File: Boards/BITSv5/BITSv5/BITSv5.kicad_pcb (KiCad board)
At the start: 4 copper layers, 54 x 59.5 mm, 80 parts, among them J1 Conn_01x10_Pin, J2 USB_C_Receptacle_USB2.0, J3 Conn_01x07, Q1 Q_NMOS_GSD, Q2 Q_PMOS_GSD, SW3 SLIDE, U1 MCU_RaspberryPi_RP2040_RP2040, U10 USBLC6-2SC6, U2 W25Q128JVS, U3 MAX-M10S, U4 MAX25255AFDA/VY+, U6 XBee_SMT, U7 TPS2121RUXR, U8 LT6703CDC-3, U9 TVS1800DRVR, Y1 12MHz

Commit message: BITSv5 board done
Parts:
- moved AE1 0.46 mm to (190.1, 103.1)
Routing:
- net GND: track 149.7 -> 119.7 mm, vias 62 -> 82
- net VCC: track 38.9 -> 13.7 mm, vias 7 -> 9
- net /IRIDIUM_TXD: track 13.9 -> 27.1 mm, vias 1 -> 0
- net +3V3: track 83.1 -> 76.0 mm, vias 22 -> 21
- net Net-(AE1-A): track 5.45 -> 11.8 mm
- net Net-(SW3-C): track 62.6 -> 59.5 mm, vias 2 -> 3
- net +5V: track 41.2 -> 42.7 mm, vias 6 -> 7
- net /XBEE_RTS: track 47.8 -> 49.1 mm
- net /GPS_SDA: track 25.0 -> 23.9 mm
- net /GPS_SCL: track 22.6 -> 21.5 mm
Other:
- board size 54 x 59.5 mm -> 63.7 x 59.5 mm

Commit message: xbee joint and bits updates
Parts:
- R17: value 51.1K -> 46.4K
- R18: value 1.05M -> 1.5M
- R19: value 154K -> 100K
- moved AE1 1.58 mm to (188.5, 103.1)
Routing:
- net +1V1: track 10.2 -> 32.2 mm, vias 1 -> 3
- net Net-(AE1-A): track 11.8 -> 10.2 mm
- net GND: track 119.7 -> 119.6 mm, vias 82 -> 109
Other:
- board size 63.7 x 59.5 mm -> 61.7 x 59.5 mm
- board text added: "A. Takeuchi J. Molter"
- board text added: "BITSv5.0 09/23"
- board text added: "J. Bishop M. Shipman"

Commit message: added button to BITS5
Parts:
- added SW1: SW_Push, Button_Switch_SMD:SW_Push_1P1T-SH_NO_CK_KMR2xxG, F.Cu at (167.6, 113.5)
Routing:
- net GND: track 119.6 -> 125.3 mm, vias 109 -> 110
- net Net-(Q2-D): track 15.5 -> 21.1 mm
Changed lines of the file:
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@@
       (net 4 "GND") (pinfunction "PAD") (pintype "unspecified"))
   )
+  (footprint "Button_Switch_SMD:SW_Push_1P1T-SH_NO_CK_KMR2xxG" (layer "F.Cu")
+    (at 167.6 113.5)
+    (descr "CK components KMR2 tactile switch with ground pin http://www.ckswitches.com/media/1479/kmr2.pdf")
+    (tags "tactile switch kmr2")
+    (property "Sheetfile" "BITSv5.kicad_sch")
+    (property "Sheetname" "")
+    (property "ki_description" "Push button switch, generic, two pins")
+    (property "ki_keywords" "switch normally-open pushbutton push-button")
+    (attr smd)
+    (fp_text reference "SW1" (at 0 -2.45) (layer "F.SilkS")
+        (effects (font (size 0.8 0.8) (thickness 0.15)))
+    )
+    (fp_text value "SW_Push" (at 0 2.55) (layer "F.Fab")
+        (effects (font (size 1 1) (thickness 0.15)))
+    )
+    (fp_text user "${REFERENCE}" (at 0 -2.45) (layer "F.Fab")
+        (effects (font (size 1 1) (thickness 0.15)))
+    )
+    (fp_line (start -2.2 0.05) (end -2.2 -0.05)
+      (stroke (width 0.12) (type solid)) (layer "F.SilkS"))
+    (fp_line (start -2.2 1.55) (end 2.2 1.55)
+      (stroke (width 0.12) (type solid)) (layer "F.SilkS"))
+    (fp_line (start -1.15 -1.55) (end -2.2 -1.55)
+      (stroke (width 0.12) (type solid)) (layer "F.SilkS"))
+    (fp_line (start 2.2 -1.55) (end 1.15 -1.55)
+      (stroke (width 0.12) (type solid)) (layer "F.SilkS"))
+    (fp_line (start 2.2 0.05) (end 2.2 -0.05)
+      (stroke (width 0.12) (type solid)) (layer "F.SilkS"))
+    (fp_line (start -2.8 -1.8) (end 2.8 -1.8)
+      (stroke (width 0.05) (type solid)) (layer "F.CrtYd"))
+    (fp_line (start -2.8 1.8) (end -2.8 -1.8)
+      (stroke (width 0.05) (type solid)) (layer "F.CrtYd"))
+    (fp_line (start 2.8 -1.8) (end 2.8 1.8)
+      (stroke (width 0.05) (type solid)) (layer "F.CrtYd"))
+    (fp_line (start 2.8 1.8) (end -2.8 1.8)
+      (stroke (width 0.05) (type solid)) (layer "F.CrtYd"))
+    (fp_line (start -2.1 -1.4) (end 2.1 -1.4)
+      (stroke (width 0.1) (type solid)) (layer "F.Fab"))
+    (fp_line (start -2.1 1.4) (end -2.1 -1.4)
+      (stroke (width 0.1) (type solid)) (layer "F.Fab"))
+    (fp_line (start 2.1 -1.4) (end 2.1 1.4)
+      (stroke (width 0.1) (type solid)) (layer "F.Fab"))
+    (fp_line (start 2.1 1.4) (end -2.1 1.4)
+      (stroke (width 0.1) (type solid)) (layer "F.Fab"))
+    (fp_circle (center 0 0) (end 0 0.8)
+      (stroke (width 0.1) (type solid)) (fill none) (layer "F.Fab"))
+    (pad "1" smd rect (at -2.05 -0.8) (size 0.9 1) (layers "F.Cu" "F.Paste" "F.Mask")
+      (net 4 "GND") (pinfunction "1") (pintype "passive"))
+    (pad "1" smd rect (at 2.05 -0.8) (size 0.9 1) (layers "F.Cu" "F.Paste" "F.Mask")
+      (net 4 "GND") (pinfunction "1") (pintype "passive"))
+    (pad "2" smd rect (at -2.05 0.8) (size 0.9 1) (layers "F.Cu" "F.Paste" "F.Mask")
+      (net 100 "Net-(Q2-D)") (pinfunction "2") (pintype "passive"))
+    (pad "2" smd rect (at 2.05 0.8) (size 0.9 1) (layers "F.Cu" "F.Paste" "F.Mask")
+      (net 100 "Net-(Q2-D)") (pinfunction "2") (pintype "passive"))
+    (pad "SH" smd rect (at 0 -1.425) (size 1.7 0.55) (layers "F.Cu" "F.Paste" "F.Mask"))
+    (model "${KICAD6_3DMODEL_DIR}/Button_Switch_SMD.3dshapes/SW_Push_1P1T-SH_NO_CK_KMR2xxG.wrl"
+      (offset (xyz 0 0 0))
+      (scale (xyz 1 1 1))
+      (rotate (xyz 0 0 0))
+    )
+  )
   (footprint "Resistor_SMD:R_0603_1608Metric_Pad0.98x0.95mm_HandSolder" (layer "F.Cu")
     (at 156.3 84.314999 180)
@@
     (property "ki_keywords" "cap capacitor")
     (attr smd)
-    (fp_text reference "C1" (at 1.12 1.445 180) (layer "F.SilkS")
+    (fp_text reference "C1" (at 1.36 1.5 180) (layer "F.SilkS")
         (effects (font (size 0.75 0.75) (thickness 0.125)))
     )
@@
   (segment (start 156.055 111.65) (end 157.055 110.65) (width 0.2) (layer "F.Cu") (net 4))
   (segment (start 178.57675 72.49075) (end 179.94 73.854) (width 0.5) (layer "F.Cu") (net 4))
+  (segment (start 169.65 112.7) (end 165.55 112.7) (width 0.25) (layer "F.Cu") (net 4))
   (segment (start 134.991899 103.068101) (end 134.991899 104.71) (width 0.5) (layer "F.Cu") (net 4))
   (segment (start 160.8 77.227499) (end 159.6625 77.227499) (width 0.5) (layer "F.Cu") (net 4))
@@
   (segment (start 159.6625 77.227499) (end 159.425 77.464999) (width 0.5) (layer "F.Cu") (net 4))
   (segment (start 176.34 114) (end 174.009998 116.330002) (width 0.5) (layer "F.Cu") (net 4))
+  (segment (start 170.7 112.7) (end 171.1 113.1) (width 0.25) (layer "F.Cu") (net 4))
   (segment (start 158.655 119.7) (end 157.34 118.385) (width 0.3) (layer "F.Cu") (net 4))
   (segment (start 153.2375 77.789999) (end 153.2625 77.764999) (width 0.5) (layer "F.Cu") (net 4))
@@
   (segment (start 151.185001 66.205001) (end 151.185001 67.242499) (width 0.5) (layer "F.Cu") (net 4))
   (segment (start 149.210001 66.260001) (end 149.210001 67.242499) (width 0.5) (layer "F.Cu") (net 4))
+  (segment (start 169.65 112.7) (end 170.7 112.7) (width 0.25) (layer "F.Cu") (net 4))
   (segment (start 180.31675 66.83825) (end 180.31925 66.84075) (width 0.5) (layer "F.Cu") (net 4))
   (segment (start 151.852501 80.88) (end 146.86 80.88) (width 1) (layer "F.Cu") (net 4))
@@
   (via (at 170.14 74.9) (size 0.5) (drill 0.3) (layers "F.Cu" "B.Cu") (free) (net 4))
   (via (at 175.31 100.94) (size 0.5) (drill 0.3) (layers "F.Cu" "B.Cu") (free) (net 4))
+  (via (at 171.1 113.1) (size 0.8) (drill 0.4) (layers "F.Cu" "B.Cu") (net 4))
   (via (at 182.45 102.09) (size 0.5) (drill 0.3) (layers "F.Cu" "B.Cu") (free) (net 4))
   (via (at 166.06 71.92) (size 0.5) (drill 0.3) (layers "F.Cu" "B.Cu") (free) (net 4))
@@
   (segment (start 151.1925 81.7675) (end 149.93 83.03) (width 0.4) (layer "B.Cu") (net 91))
   (segment (start 159.513263 113.9) (end 161.69 113.9) (width 0.2) (layer "F.Cu") (net 100))
+  (segment (start 165.55 114.3) (end 165.98875 114.3) (width 0.25) (layer "F.Cu") (net 100))
   (segment (start 161.69 113.9) (end 162.21 113.38) (width 0.2) (layer "F.Cu") (net 100))
+  (segment (start 169.65 114.3) (end 169.58875 114.3) (width 0.25) (layer "F.Cu") (net 100))
   (segment (start 167.78875 116.1) (end 167.78875 117.2875) (width 0.5) (layer "F.Cu") (net 100))
+  (segment (start 165.98875 114.3) (end 167.78875 116.1) (width 0.25) (layer "F.Cu") (net 100))
   (segment (start 167.78875 117.2875) (end 164.80125 117.2875) (width 0.5) (layer "F.Cu") (net 100))
   (segment (start 164.80125 117.2875) (end 164.53875 117.55) (width 0.5) (layer "F.Cu") (net 100))
+  (segment (start 169.58875 114.3) (end 167.78875 116.1) (width 0.25) (layer "F.Cu") (net 100))
   (segment (start 158.855 113.241737) (end 159.513263 113.9) (width 0.2) (layer "F.Cu") (net 100))
   (segment (start 158.855 112.8125) (end 158.855 113.241737) (width 0.2) (layer "F.Cu") (net 100))

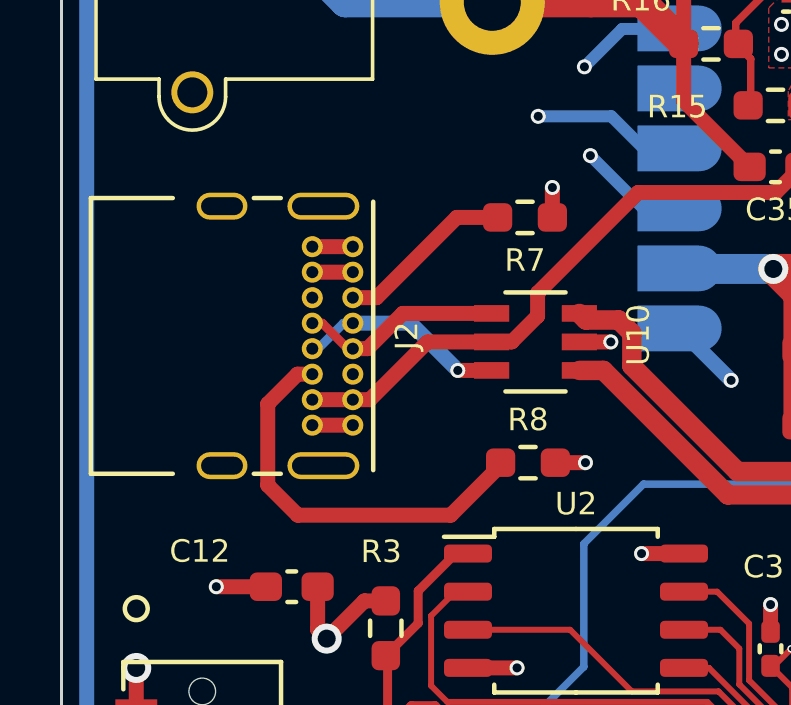
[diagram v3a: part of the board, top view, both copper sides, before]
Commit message: BITSv5 USB change
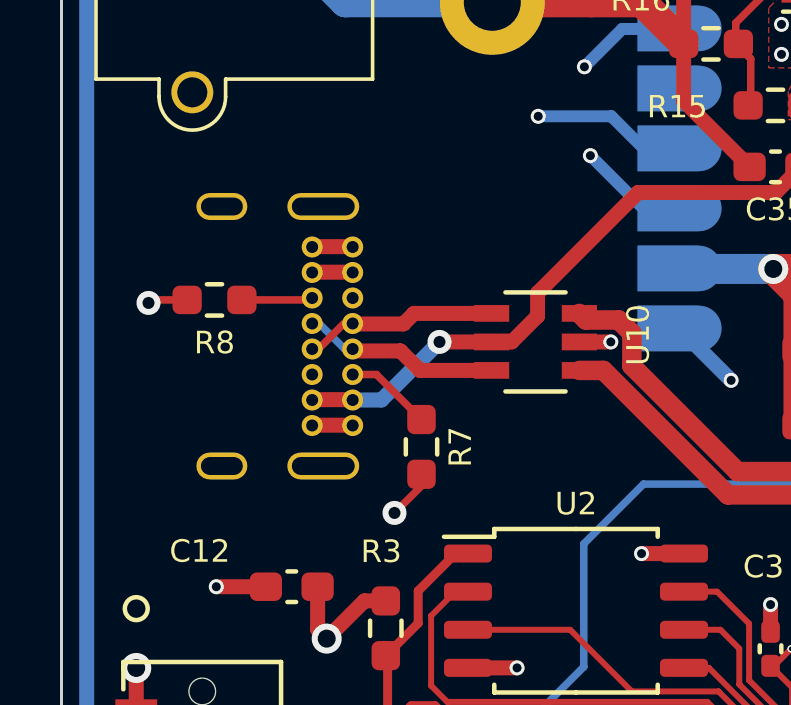
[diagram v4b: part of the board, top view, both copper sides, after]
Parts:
- J2: moved to B.Cu
- moved R8 11.8 mm to (137.6, 90.8), turned to 180 degrees
- moved R7 8.39 mm to (144.5, 95.7), turned to 90 degrees
- moved J2 5.96 mm to (142.2, 95.0), turned to 90 degrees
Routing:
- net Net-(J2-CC2): track 13.6 -> 2.37 mm
- net Net-(J2-CC1): track 6.02 -> 2.92 mm
- net GND: track 125.3 -> 126.3 mm
- net VBUS: track 29.6 -> 29.2 mm, vias 0 -> 1
- net Net-(J2-D+-PadA6): track 6.98 -> 6.63 mm, vias 1 -> 0

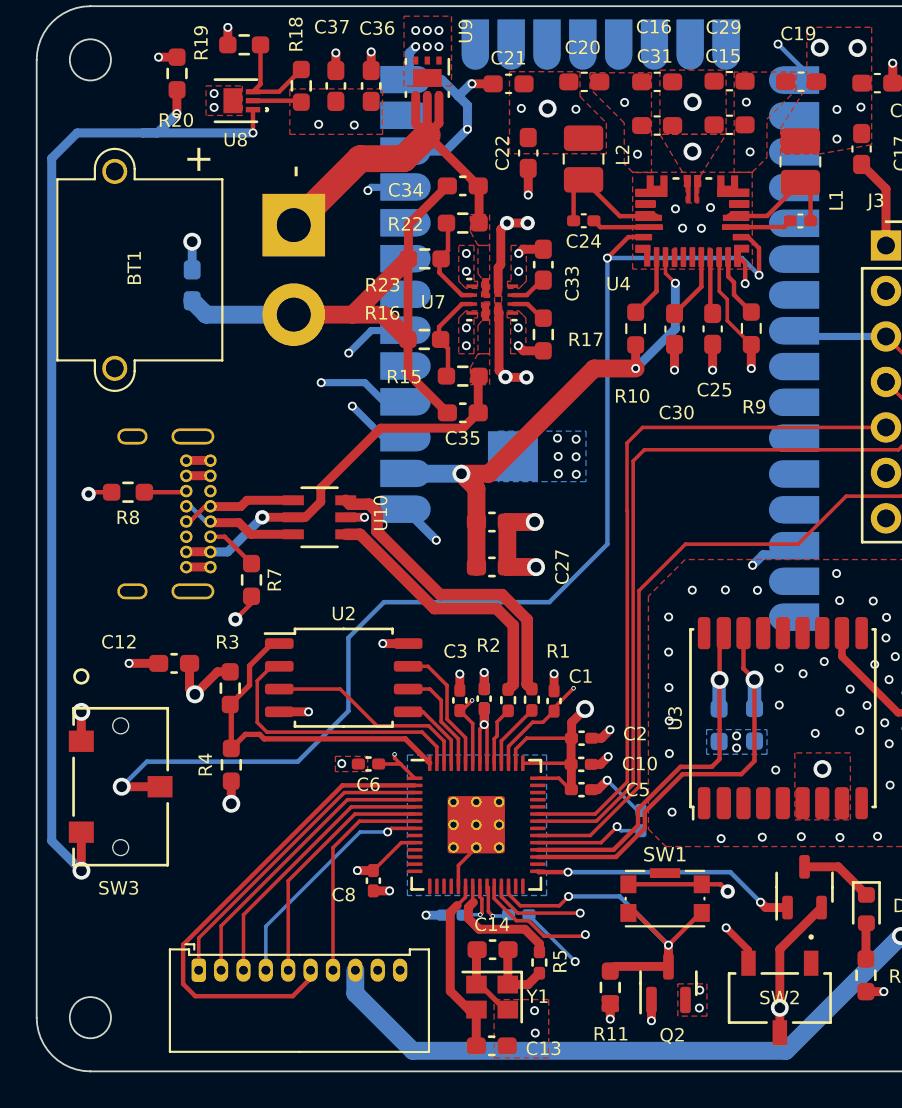
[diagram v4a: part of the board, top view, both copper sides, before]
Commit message: BITSv5 added additional Xbee connector
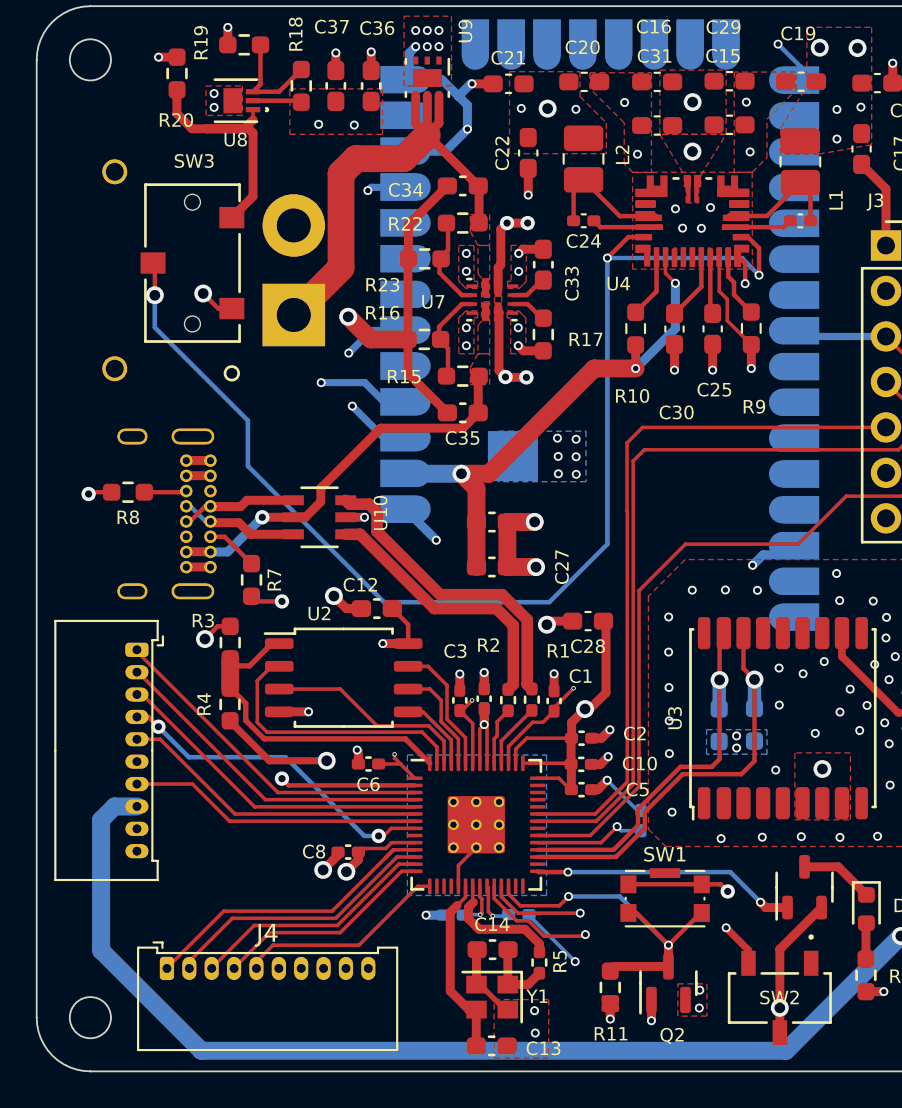
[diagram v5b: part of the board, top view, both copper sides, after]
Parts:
- added J4: Conn_01x10_Pin, Connector_Molex:Molex_PicoBlade_53048-1010_1x10_P1.25mm_Horizontal, F.Cu at (139.8, 117.4)
- BT1: moved to B.Cu
- C28: moved to F.Cu
- moved SW3 29.5 mm to (141.2, 78.0), turned to 90 degrees
- moved C28 29.0 mm to (163.3, 98.0), turned to 180 degrees
- moved J1 18.2 mm to (138.1, 99.6), turned to -90 degrees
- moved C12 11.7 mm to (151.5, 97.3)
- moved BT1 5.02 mm to (146.9, 80.9), turned to -90 degrees
- moved R4 3.37 mm to (143.3, 102.7)
- moved R3 2.55 mm to (143.3, 99.2)
- moved C8 2.13 mm to (149.9, 110.9), turned to 180 degrees
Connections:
- U1 pad 11: unconnected-(U1-GPIO8-Pad11) -> /2.4_MISO
- U1 pad 12: unconnected-(U1-GPIO9-Pad12) -> /2.4_SSEL
- U1 pad 13: unconnected-(U1-GPIO10-Pad13) -> /2.4_SCLK
- U1 pad 14: unconnected-(U1-GPIO11-Pad14) -> /2.4_MOSI
- U1 pad 15: unconnected-(U1-GPIO12-Pad15) -> /2.4_ATTN
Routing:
- net Net-(SW3-C): track 59.5 -> 17.3 mm, vias 3 -> 0
- net +5V: track 42.7 -> 66.2 mm
- net /2.4_MISO: track 0.00 -> 17.2 mm
- net /2.4_SSEL: track 0.00 -> 15.0 mm
- net /2.4_SCLK: track 0.00 -> 13.8 mm
- net GND: track 126.3 -> 112.9 mm, vias 110 -> 112
- net /2.4_MOSI: track 0.00 -> 12.4 mm
- net /2.4_ATTN: track 0.00 -> 11.8 mm
- net /IRIDIUM_TXD: track 27.1 -> 16.1 mm, vias 0 -> 1
- net Net-(SW2-B): track 52.0 -> 61.7 mm
- net /IRIDIUM_NETAV: track 13.0 -> 18.4 mm, vias 1 -> 2
- net +BATT: track 22.8 -> 28.0 mm
- net +3V3: track 76.0 -> 80.6 mm, vias 21 -> 20
- net /IRIDIUM_ON/OFF: track 12.0 -> 16.4 mm
- net /IRIDIUM_RING: track 13.6 -> 17.2 mm
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
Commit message: bits v5 w/ dorji radio
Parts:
- removed C31: 0.1uF, Capacitor_SMD:C_0603_1608Metric_Pad1.08x0.95mm_HandSolder
- removed J4: Conn_01x10_Pin, Connector_Molex:Molex_PicoBlade_53048-1010_1x10_P1.25mm_Horizontal
- removed Q2: Q_PMOS_GSD, Package_TO_SOT_SMD:SOT-23
- added AE2: Antenna, BITSv5:ANT_0915AT43A0026E_JOT, F.Cu at (150.4, 73.0)
- added BT2: 3V, BITSv5:SEIKO_ML414H_IV01E, B.Cu at (148.7, 51.4)
- added C38: 15uF, Capacitor_SMD:C_1206_3216Metric, F.Cu at (149.5, 61.7)
- added C39: 1uF, Capacitor_SMD:C_0603_1608Metric, F.Cu at (140.5, 46.9)
- added C40: 1uF, Capacitor_SMD:C_0603_1608Metric, F.Cu at (138.9, 46.9)
- added C41: 1uF, Capacitor_SMD:C_0603_1608Metric, F.Cu at (134.6, 75.2)
- added C42: 100nF, Capacitor_SMD:C_0603_1608Metric, F.Cu at (141.2, 74.5)
- added C43: 200nF, Capacitor_SMD:C_0603_1608Metric, F.Cu at (141.2, 72.9)
- added D2: 0.5A/40V/240mV, Diode_SMD:D_SOD-123F, F.Cu at (147.4, 52.1)
- added H1: M2, MountingHole:MountingHole_2.2mm_M2_Pad, F.Cu at (108.2, 45.2)
- added H2: M2, MountingHole:MountingHole_2.2mm_M2_Pad, F.Cu at (108.2, 84.2)
- added H3: M2, MountingHole:MountingHole_2.2mm_M2_Pad, F.Cu at (149.2, 84.2)
- added H4: M2, MountingHole:MountingHole_2.2mm_M2_Pad, F.Cu at (149.2, 45.2)
- added L3: 3.3uH, Inductor_SMD:L_1210_3225Metric, F.Cu at (146.0, 56.1)
- added L4: 3.3uH, Inductor_SMD:L_1210_3225Metric, F.Cu at (145.9, 62.4)
- added R13: 100m, Resistor_SMD:R_0603_1608Metric, F.Cu at (145.1, 60.0)
- added R14: 3.3K, Resistor_SMD:R_0603_1608Metric, F.Cu at (149.4, 51.4)
- added R27: 22.1K, Resistor_SMD:R_0603_1608Metric, F.Cu at (139.2, 52.1)
- added R29: 100K, Resistor_SMD:R_0603_1608Metric, F.Cu at (137.3, 61.6)
- added R32: 34.8K, Resistor_SMD:R_0603_1608Metric, F.Cu at (135.2, 52.2)
- added R33: 100K, Resistor_SMD:R_0603_1608Metric, F.Cu at (135.7, 61.6)
- added R34: 15K, Resistor_SMD:R_0603_1608Metric, F.Cu at (133.2, 55.4)
- added R6: 10K, Resistor_SMD:R_0603_1608Metric, B.Cu at (116.1, 81.7)
- added U11: MS5607-02BA, Package_LGA:LGA-8_3x5mm_P1.25mm, B.Cu at (117.7, 79.0)
- added U5: LT8653SIV-PBF, BITSv5:LT8653SIV-PBF, F.Cu at (137.2, 57.8)
- AE1, R7, R8, U3: moved to B.Cu
- BT1: moved to F.Cu
- C1, C10, C2, C3, C5, C6, C7, C8: footprint Capacitor_SMD:C_0402_1005Metric_Pad0.74x0.62mm_HandSolder -> Capacitor_SMD:C_0402_1005Metric
- C11, C32, C4, C9: footprint Capacitor_SMD:C_0402_1005Metric_Pad0.74x0.62mm_HandSolder -> Capacitor_SMD:C_0402_1005Metric; moved to F.Cu
- C12, C13, C14, C37: footprint Capacitor_SMD:C_0603_1608Metric_Pad1.08x0.95mm_HandSolder -> Capacitor_SMD:C_0402_1005Metric
- C15: value 0.1uF -> 4.7uF; footprint Capacitor_SMD:C_0603_1608Metric_Pad1.08x0.95mm_HandSolder -> Capacitor_SMD:C_0603_1608Metric
- C16: value 4.7uF -> 47uF; footprint Capacitor_SMD:C_0603_1608Metric_Pad1.08x0.95mm_HandSolder -> Capacitor_SMD:C_1206_3216Metric
- C17: value 22uF -> 4.7pF; footprint Capacitor_SMD:C_0603_1608Metric_Pad1.08x0.95mm_HandSolder -> Capacitor_SMD:C_0603_1608Metric
- C18, C21: value 22uF -> 470pF; footprint Capacitor_SMD:C_0603_1608Metric_Pad1.08x0.95mm_HandSolder -> Capacitor_SMD:C_0603_1608Metric
- C19: value 22uF -> 10nF; footprint Capacitor_SMD:C_0603_1608Metric_Pad1.08x0.95mm_HandSolder -> Capacitor_SMD:C_0603_1608Metric
- C20: value 22uF -> 100uF; footprint Capacitor_SMD:C_0603_1608Metric_Pad1.08x0.95mm_HandSolder -> Capacitor_SMD:C_1206_3216Metric
- C22: value 22uF -> 100nF; footprint Capacitor_SMD:C_0603_1608Metric_Pad1.08x0.95mm_HandSolder -> Capacitor_SMD:C_0603_1608Metric
- C23: value 0.1uF -> 4.7pF; footprint Capacitor_SMD:C_0402_1005Metric_Pad0.74x0.62mm_HandSolder -> Capacitor_SMD:C_0603_1608Metric
- C24: value 0.1uF -> 10nF; footprint Capacitor_SMD:C_0402_1005Metric_Pad0.74x0.62mm_HandSolder -> Capacitor_SMD:C_0603_1608Metric
- C25: value 2.2uF -> 1uF; footprint Capacitor_SMD:C_0603_1608Metric_Pad1.08x0.95mm_HandSolder -> Capacitor_SMD:C_0603_1608Metric
- C26: value 100pF -> 10uF; footprint Capacitor_SMD:C_0603_1608Metric_Pad1.08x0.95mm_HandSolder -> Capacitor_SMD:C_0603_1608Metric
- C27, C33, C34, C35, C36: footprint Capacitor_SMD:C_0603_1608Metric_Pad1.08x0.95mm_HandSolder -> Capacitor_SMD:C_0603_1608Metric
- C28: value 10uF -> 15uF; footprint Capacitor_SMD:C_0603_1608Metric_Pad1.08x0.95mm_HandSolder -> Capacitor_SMD:C_1206_3216Metric
- C29: value 4.7uF -> 100nF; footprint Capacitor_SMD:C_0603_1608Metric_Pad1.08x0.95mm_HandSolder -> Capacitor_SMD:C_0603_1608Metric; moved to B.Cu
- C30: value 4.7uF -> 100nF; footprint Capacitor_SMD:C_0603_1608Metric_Pad1.08x0.95mm_HandSolder -> Capacitor_SMD:C_0603_1608Metric
- J1: footprint Connector_Molex:Molex_PicoBlade_53048-1010_1x10_P1.25mm_Horizontal -> Connector_Molex:Molex_PicoBlade_53261-1071_1x10-1MP_P1.25mm_Horizontal
- J2: footprint Connector_USB:USB_C_Receptacle_GCT_USB4085 -> Connector_USB:USB_C_Receptacle_GCT_USB4105-xx-A_16P_TopMnt_Horizontal; moved to F.Cu
- J3: value Conn_01x07 -> SOICbite; footprint Connector_PinSocket_2.54mm:PinSocket_1x07_P2.54mm_Vertical -> BITSv5:SOIC_clipProgSmall
- L1, L2: value 0.47uH -> 2.2uH; footprint Inductor_SMD:L_1008_2520Metric_Pad1.43x2.20mm_HandSolder -> Inductor_SMD:L_1210_3225Metric
- R1, R2: value 27Ω -> 27; footprint Resistor_SMD:R_0402_1005Metric_Pad0.72x0.64mm_HandSolder -> Resistor_SMD:R_0402_1005Metric
- R10: value 10K -> 100m; footprint Resistor_SMD:R_0603_1608Metric_Pad0.98x0.95mm_HandSolder -> Resistor_SMD:R_0603_1608Metric
- R11: value 10K -> 100K; footprint Resistor_SMD:R_0603_1608Metric_Pad0.98x0.95mm_HandSolder -> Resistor_SMD:R_0603_1608Metric
- R12, R15, R16, R22, R23, R4: footprint Resistor_SMD:R_0603_1608Metric_Pad0.98x0.95mm_HandSolder -> Resistor_SMD:R_0603_1608Metric
- R17: value 46.4K -> 44.2K; footprint Resistor_SMD:R_0603_1608Metric_Pad0.98x0.95mm_HandSolder -> Resistor_SMD:R_0603_1608Metric
- R18, R19, R20: footprint Resistor_SMD:R_0603_1608Metric_Pad0.98x0.95mm_HandSolder -> Resistor_SMD:R_0402_1005Metric
- R21, R24: footprint Resistor_SMD:R_0603_1608Metric_Pad0.98x0.95mm_HandSolder -> Resistor_SMD:R_0603_1608Metric; moved to F.Cu
- R3: value 10K -> DNF; footprint Resistor_SMD:R_0603_1608Metric_Pad0.98x0.95mm_HandSolder -> Resistor_SMD:R_0603_1608Metric
- R5: footprint Resistor_SMD:R_0402_1005Metric_Pad0.72x0.64mm_HandSolder -> Capacitor_SMD:C_0402_1005Metric
- R9: footprint Resistor_SMD:R_0603_1608Metric_Pad0.98x0.95mm_HandSolder -> Resistor_SMD:R_0603_1608Metric; moved to B.Cu
- U10: footprint BITSv5:SOT23-6L_STM-M -> BITSv5:SOT23-6L_STM
- U2: footprint Package_SO:SOIC-8_5.23x5.23mm_P1.27mm -> BITSv5:WSON_128JVPIQ_WIN
- U4: value MAX25255AFDA/VY+ -> DRF1262TL; footprint BITSv5:21-100477_90-100168_MXM -> BITSv5:DRF1262TL; moved to B.Cu
- U6: value XBee_SMT -> TPS2121RUXR; footprint BITSv5:XCVR_XBP9X-DMUS-001 -> BITSv5:TPS2121; moved to F.Cu
- U7: value TPS2121RUXR -> MAX6747KA29+T; footprint BITSv5:TPS2121 -> BITSv5:21-0078H_MXM
- moved AE1 85.5 mm to (126.6, 44.2), turned to 180 degrees
- moved R12 75.1 mm to (115.9, 76.8)
- moved J3 73.2 mm to (115.0, 43.3), turned to 180 degrees
- moved D1 71.5 mm to (118.4, 76.0), turned to 180 degrees
- moved Q1 69.9 mm to (117.7, 73.3), turned to 0 degrees
- moved U3 64.8 mm to (139.9, 48.5)
- moved R21 64.6 mm to (142.0, 46.9)
- moved R24 63.0 mm to (143.6, 46.9)
- moved C32 61.8 mm to (126.7, 61.7)
- moved C4 58.3 mm to (124.0, 68.1), turned to 180 degrees
- moved C13 57.6 mm to (136.0, 68.5), turned to -90 degrees
- moved C2 56.9 mm to (124.2, 62.8), turned to 180 degrees
- moved SW2 56.3 mm to (133.3, 80.1)
- moved R5 55.9 mm to (135.5, 67.1), turned to 180 degrees
- moved C8 54.9 mm to (125.7, 61.7), turned to 90 degrees
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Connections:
- net /GPS_SCL renamed /SCL
- net /XOUT renamed Net-(U1-XOUT)
- C13 pad 1: GND -> Net-(U1-XIN)
- C13 pad 2: /XIN -> GND
- C14 pad 1: GND -> Net-(C14-Pad1)
- C14 pad 2: Net-(C14-Pad2) -> GND
- C15 pad 1: GND -> VCC
- C15 pad 2: VCC -> GND
- C16 pad 1: VCC -> Net-(U5-FB1)
- C17 pad 1: GND -> Net-(U5-VC1)
- C17 pad 2: +5V -> GND
- C18 pad 1: GND -> Net-(C18-Pad1)
- C18 pad 2: +5V -> GND
- C19 pad 1: GND -> Net-(U5-SS1)
- C19 pad 2: +5V -> GND
- C20 pad 1: GND -> Net-(U5-BIAS)
- C20 pad 2: +3V3 -> GND
- C21 pad 1: GND -> Net-(C21-Pad1)
- C21 pad 2: +3V3 -> GND
- C22 pad 1: GND -> VCC
- C22 pad 2: +3V3 -> GND
- C23 pad 1: Net-(U4-BST2) -> Net-(U5-VC2)
- C23 pad 2: Net-(U4-LX2) -> GND
- C24 pad 1: Net-(U4-BST1) -> Net-(U5-SS2)
- C24 pad 2: Net-(U4-LX1) -> GND
- C25 pad 1: GND -> Net-(U5-VCC)
- C25 pad 2: Net-(U4-EXTVCC) -> GND
- C26 pad 1: +3V3 -> +5V
- C27 pad 1: +3V3 -> +5V
- C29 pad 1: GND -> +3V3
- C29 pad 2: VCC -> GND
- C30 pad 1: GND -> Net-(U7-*MR)
- C30 pad 2: Net-(U4-BIAS) -> GND
- C33 pad 1: Net-(U7-SS) -> Net-(U6-SS)
- J1 pad 7: /IRIDIUM_ON/OFF -> /RESET
- J3 pad 1: GND -> /RP_SWCLK
- J3 pad 2: /XBEE_DTR -> /RP_SWD
- J3 pad 3: /XBEE_RTS -> unconnected-(J3-Pin_3-Pad3)
- J3 pad 4: /XBEE_DIN -> unconnected-(J3-Pin_4-Pad4)
- J3 pad 5: /XBEE_DOUT -> unconnected-(J3-Pin_5-Pad5)
- J3 pad 6: /RP_SWD -> unconnected-(J3-Pin_6-Pad6)
- J3 pad 7: /RP_SWCLK -> unconnected-(J3-Pin_7-Pad7)
- L1 pad 1: +5V -> Net-(U5-FB1)
- L1 pad 2: Net-(U4-LX2) -> Net-(U5-SW1)
- L2 pad 1: Net-(U4-LX1) -> Net-(U5-BIAS)
- L2 pad 2: +3V3 -> Net-(U5-SW2)
- R10 pad 2: Net-(U4-PGOOD1) -> Net-(U5-BIAS)
- R11 pad 2: Net-(Q2-D) -> /RESET
- R15 pad 2: Net-(U7-OV1) -> Net-(U6-OV1)
- R16 pad 1: Net-(U7-OV1) -> Net-(U6-OV1)
- R17 pad 1: Net-(U7-ILM) -> Net-(U6-ILM)
- R21 pad 2: /GPS_SDA -> /SDA
- R22 pad 2: Net-(U7-OV2) -> Net-(U6-OV2)
- R23 pad 1: Net-(U7-OV2) -> Net-(U6-OV2)
- R5 pad 1: Net-(C14-Pad2) -> Net-(C14-Pad1)
- R9 pad 1: +5V -> +3V3
- R9 pad 2: Net-(U4-PGOOD2) -> /SDA
- SW1 pad 2: Net-(Q2-D) -> Net-(U7-*MR)
- U1 pad 11: /2.4_MISO -> /DRF_TXEN
- U1 pad 12: /2.4_SSEL -> /DRF_SW
- U1 pad 13: /2.4_SCLK -> /DRF_DIO1
- U1 pad 14: /2.4_MOSI -> /DRF_BUSY
- U1 pad 15: /2.4_ATTN -> /IRIDIUM_TXD
- U1 pad 16: unconnected-(U1-GPIO13-Pad16) -> /WATCHDOG
- U1 pad 2: /IRIDIUM_TXD -> /LED
- U1 pad 20: /XIN -> Net-(U1-XIN)
- U1 pad 26: Net-(Q2-D) -> /RESET
- U1 pad 29: /LED -> unconnected-(U1-GPIO18-Pad29)
- U1 pad 31: /GPS_SDA -> /SDA
- U1 pad 34: /XBEE_RTS -> unconnected-(U1-GPIO22-Pad34)
- U1 pad 36: /XBEE_DIN -> /DRF_MISO
- U1 pad 37: /XBEE_DOUT -> /DRF_CS
- U1 pad 38: unconnected-(U1-GPIO26_ADC0-Pad38) -> /DRF_CLK
- U1 pad 39: unconnected-(U1-GPIO27_ADC1-Pad39) -> /DRF_MOSI
- U1 pad 40: /VBAT -> unconnected-(U1-GPIO28_ADC2-Pad40)
- U1 pad 6: /IRIDIUM_RING -> /IRIDIUM_NETAV
- U1 pad 7: /IRIDIUM_ON/OFF -> /IRIDIUM_RING
- U1 pad 8: /IRIDIUM_NETAV -> unconnected-(U1-GPIO6-Pad8)
- U3 pad 16: /GPS_SDA -> /SDA
- U3 pad 6: +3V3 -> Net-(BT2-+)
- U4 pad 1: +3V3 -> /DRF_SW
- U4 pad 10: unconnected-(U4-NC-Pad10) -> /RESET
- U4 pad 11: Net-(U4-LX1) -> /DRF_MISO
- U4 pad 12: Net-(U4-BST1) -> /DRF_MOSI
- U4 pad 13: /LVC_CUTOFF -> /DRF_CLK
- U4 pad 14: unconnected-(U4-SYNCOUT-Pad14) -> /DRF_CS
- U4 pad 15: Net-(U4-PGOOD1) -> GND
- U4 pad 16: +3V3 -> Net-(AE2-A)
- U4 pad 17: unconnected-(U4-TEMP-Pad17) -> GND
- U4 pad 2: /LVC_CUTOFF -> GND
- U4 pad 3: Net-(U4-BST2) -> /DRF_TXEN
- U4 pad 4: Net-(U4-LX2) -> GND
- U4 pad 5: unconnected-(U4-NC-Pad5) -> GND
- U4 pad 6: GND -> +5V
- U4 pad 7: VCC -> +5V
- U4 pad 8: VCC -> /DRF_DIO1
- U4 pad 9: GND -> /DRF_BUSY
- U6 pad 1: GND -> VCC
- U6 pad 10: /XBEE_DTR -> Net-(U6-ILM)
- U6 pad 11: GND -> Net-(U6-SS)
- U6 pad 12: unconnected-(U6-DO19/~{SPI_ATTN}-Pad12) -> GND
- U6 pad 2: +3V3 -> +BATT
- U6 pad 3: /XBEE_DOUT -> GND
- U6 pad 4: /XBEE_DIN -> Net-(U6-OV2)
- U6 pad 5: unconnected-(U6-DIO12-Pad5) -> Net-(U6-OV1)
- U6 pad 6: /XBEE_RESET -> GND
- U6 pad 7: unconnected-(U6-DIO10/RSSI/PWM0-Pad7) -> VBUS
- U6 pad 8: unconnected-(U6-DIO11/PWM1-Pad8) -> VCC
- U6 pad 9: (no net) -> GND
- U7 pad 1: VCC -> Net-(U7-*MR)
- U7 pad 2: +BATT -> Net-(U7-SWT)
- U7 pad 3: GND -> Net-(U7-SRT)
- U7 pad 4: Net-(U7-OV2) -> GND
- U7 pad 5: Net-(U7-OV1) -> +3V3
- U7 pad 6: GND -> /WATCHDOG
- U7 pad 7: VBUS -> /RESET
- U7 pad 8: VCC -> +3V3
- Y1 pad 1: Net-(C14-Pad2) -> Net-(C14-Pad1)
- Y1 pad 3: /XIN -> Net-(U1-XIN)
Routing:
- net /XBEE_RESET: track 86.1 -> 0.00 mm, vias 2 -> 0
- net /XBEE_DIN: track 81.7 -> 0.00 mm, vias 1 -> 0
- net /XBEE_DOUT: track 73.7 -> 0.00 mm, vias 1 -> 0
- net /SDA: track 0.00 -> 70.9 mm, vias 0 -> 3
- net Net-(SW2-B): track 61.7 -> 2.36 mm, vias 2 -> 0
- net /XBEE_RTS: track 49.1 -> 0.00 mm
- net /SCL: track 21.5 -> 69.9 mm, vias 1 -> 3
- net /RESET: track 0.00 -> 47.2 mm, vias 0 -> 4
- net /XBEE_DTR: track 36.4 -> 0.00 mm, vias 1 -> 0
- net +5V: track 66.2 -> 34.9 mm, vias 7 -> 15
- net Net-(SW3-C): track 17.3 -> 47.6 mm, vias 0 -> 2
- net /GPS_SDA: track 23.9 -> 0.00 mm, vias 1 -> 0
- net +BATT: track 28.0 -> 4.67 mm, vias 0 -> 2
- net /DRF_CS: track 0.00 -> 22.9 mm, vias 0 -> 1
- net /DRF_MOSI: track 0.00 -> 22.9 mm, vias 0 -> 1
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- added copper zone on B.Cu, net +5V
- added copper zone on F.Cu, net Net-(U5-BIAS)
- added copper zone on F.Cu, net Net-(U5-FB1)
- removed copper zone on In2.Cu, net VCC
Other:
- board size 61.7 x 59.5 mm -> 47 x 45 mm
- board text added: "BITSv5.0 10/2023"
- board text added: "J. Bishop M. Shipman A. Takeuchi"
- board text removed: "A. Takeuchi J. Molter"
- board text removed: "BITSv5.0 09/23"
- board text removed: "J. Bishop M. Shipman"
